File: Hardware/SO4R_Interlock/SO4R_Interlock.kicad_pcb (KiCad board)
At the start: 4 copper layers, 67.4 x 68.6 mm, 120 parts, among them J1 USB-C 2.0 16P, J2 USB-C 2.0 16P, J3 USB-C 2.0 16P, J4 USB-C 2.0 16P, J5 8P8C_LED_Shielded_x4, J7 Header 1x3, U1 FT230XS, U10 TPD4E02B04DQA, U11 TPD4E02B04DQA, U12 TPD4E02B04DQA, U2 FT230XS, U3 74LVC1G07, U4 AVR32DB48x-xPT, U5 FT230XS, U6 FT230XS, U7 74LVC1G07, U8 74LVC1G07, U9 TPD4E02B04DQA

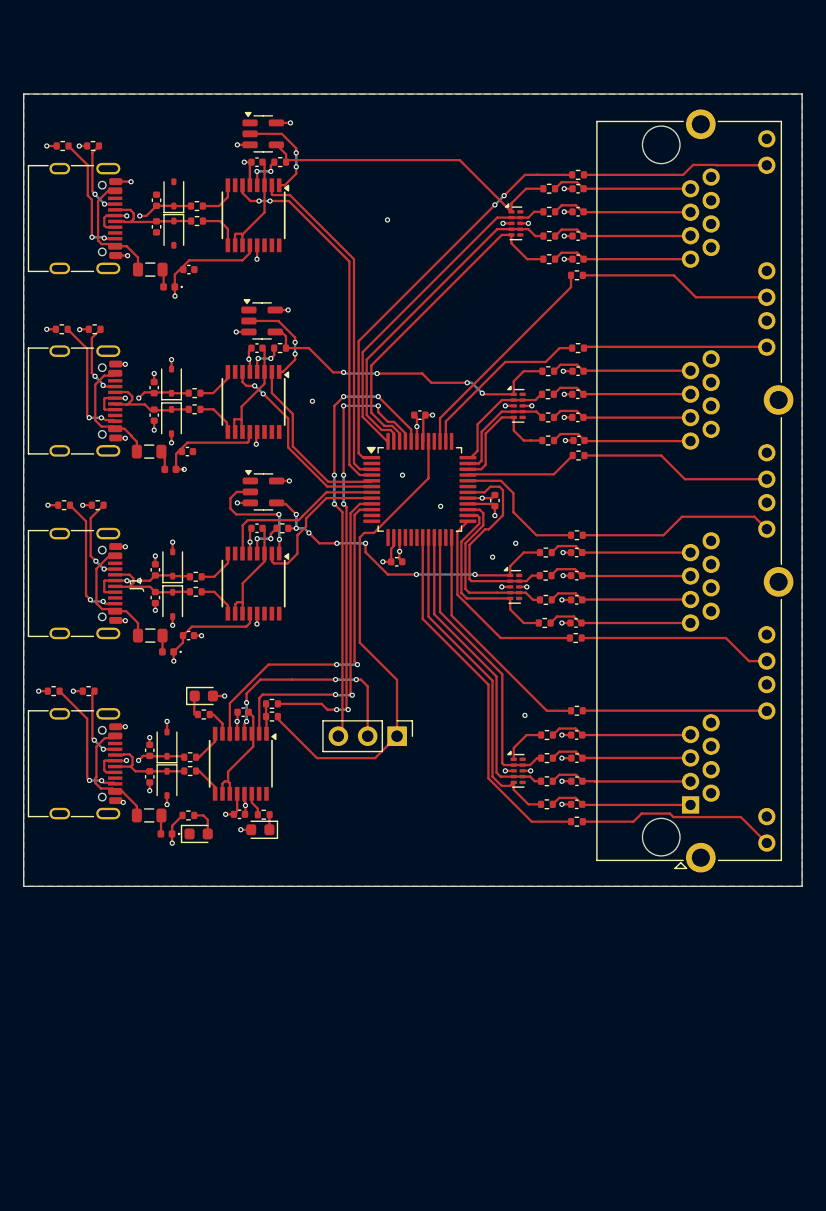
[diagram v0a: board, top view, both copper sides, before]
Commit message: Ordered V1 of Transfer Relay boards and Interlock boards and assembly
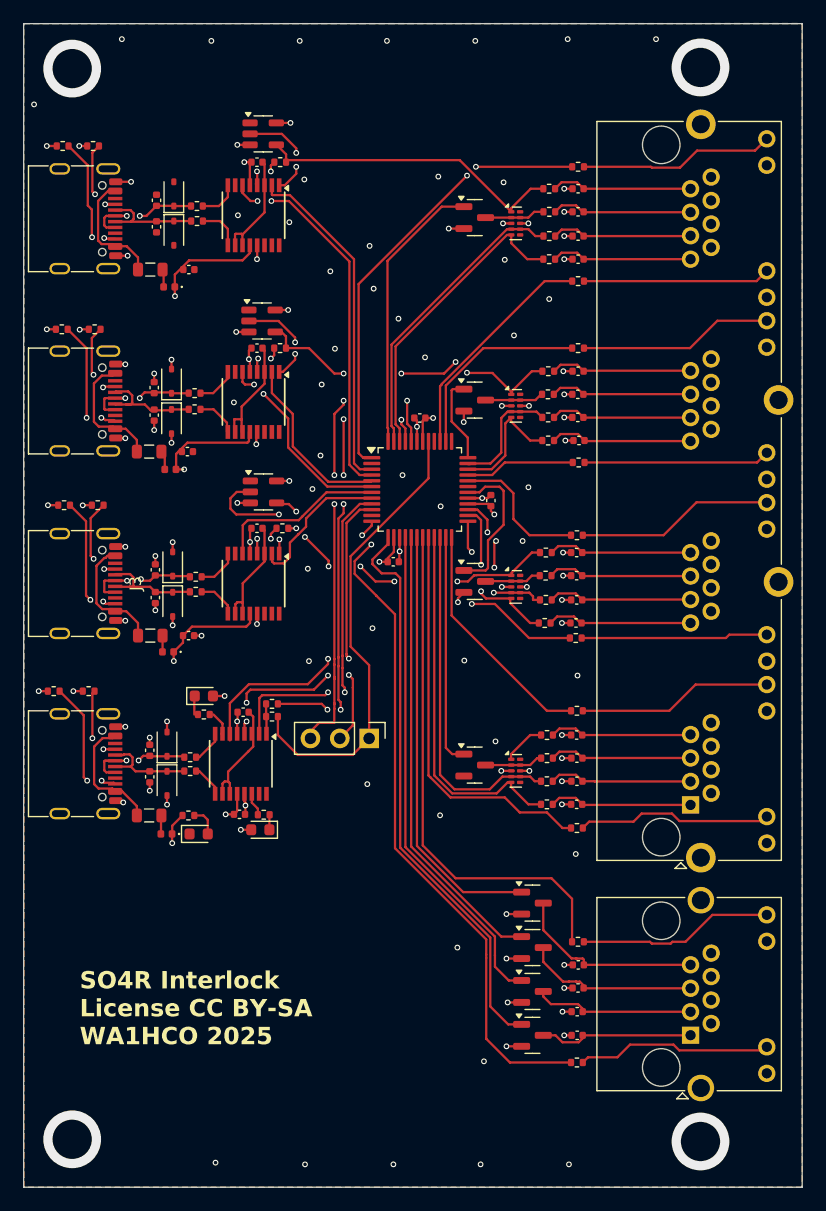
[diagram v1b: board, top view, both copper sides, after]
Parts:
- added C18: .1u, Capacitor_SMD:C_0402_1005Metric, F.Cu at (151.2, 129.5)
- added C19: .1u, Capacitor_SMD:C_0402_1005Metric, F.Cu at (151.2, 131.5)
- added C21: .1u, Capacitor_SMD:C_0402_1005Metric, F.Cu at (151.1, 133.6)
- added C22: .1u, Capacitor_SMD:C_0402_1005Metric, F.Cu at (151.1, 135.6)
- added J6: RJ45_LED_Shielded, Connector_RJ:RJ45_Amphenol_RJHSE538X, F.Cu at (160.9, 135.6)
- added Q1: 2N7002, Package_TO_SOT_SMD:SOT-23, F.Cu at (147.2, 124.2)
- added Q2: 2N7002, Package_TO_SOT_SMD:SOT-23, F.Cu at (147.2, 128.0)
- added Q3: 2N7002, Package_TO_SOT_SMD:SOT-23, F.Cu at (147.2, 131.8)
- added Q4: 2N7002, Package_TO_SOT_SMD:SOT-23, F.Cu at (147.2, 135.6)
- added Q5: 2N7002, Package_TO_SOT_SMD:SOT-23, F.Cu at (142.2, 112.2)
- added Q6: 2N7002, Package_TO_SOT_SMD:SOT-23, F.Cu at (142.2, 64.8)
- added Q7: 2N7002, Package_TO_SOT_SMD:SOT-23, F.Cu at (142.2, 80.6)
- added Q8: 2N7002, Package_TO_SOT_SMD:SOT-23, F.Cu at (142.2, 96.3)
- added R25: 1K, Resistor_SMD:R_0402_1005Metric, F.Cu at (151.1, 137.9)
- added R26: 1K, Resistor_SMD:R_0402_1005Metric, F.Cu at (151.2, 127.5)
- C24: renamed from C35; value .01 -> .1u
- C25: renamed from C28; value .01 -> .1u
- C26: renamed from C20; value .01 -> .1u
- C27: renamed from C25; value .01 -> .1u
- C28: renamed from C29; value .01 -> .1u
- C29: renamed from C30; value .01 -> .1u
- C30: renamed from C22; value .01 -> .1u
- C31: renamed from C24; value .01 -> .1u
- C32, C33: value .01 -> .1u
- C34: renamed from C27; value .01 -> .1u
- C35: renamed from C23; value .01 -> .1u
- C36: renamed from C31; value .01 -> .1u
- C37: renamed from C34; value .01 -> .1u
- C38: renamed from C26; value .01 -> .1u
- C39: renamed from C19; value .01 -> .1u
- D5: renamed from D13; value D_Schottky -> RBQ161QS-40
- R41: renamed from R27; value 33 -> 1K
- moved J5 2.42 mm to (133.1, 109.9)
- moved R44 0.70 mm to (151.2, 60.4)
- moved R45 0.60 mm to (151.2, 86.0)
- moved R49 0.55 mm to (151.1, 117.7)
- moved R43 0.51 mm to (151.2, 70.3)
- moved C17 0.35 mm to (143.7, 89.3)
- moved C20 0.30 mm to (135.2, 94.6)
- moved C23 0.25 mm to (137.5, 82.2)
- moved U10 0.21 mm to (145.8, 81.1)
- moved U12 0.21 mm to (145.8, 112.7)
- moved U11 0.09 mm to (145.8, 96.8)
- turned R47 to 180 degrees
- renumbered C14 to C1, C12 to C10, C16 to C11, C8 to C12, C17 to C13, C15 to C14, C9 to C15, C10 to C16, C21 to C17, C6 to C2, C11 to C20, C13 to C23, C2 to C4, C18 to C5, C5 to C6, C4 to C7, C1 to C8, C7 to C9, D15 to D1, D11 to D10, D6 to D11, D4 to D12, D3 to D13, D2 to D14, D8 to D15, D12 to D2, D5 to D3, D9 to D4, D7 to D6, D1 to D7, D14 to D8, D10 to D9, FB3 to FB1, FB1 to FB3, J4 to J1, J3 to J2, J1 to J3, J2 to J4, J7 to J5, J5 to J7, R8 to R1, R22 to R10, R23 to R11, R20 to R12, R21 to R13, R11 to R14, R18 to R15, R13 to R16, R12 to R17, R14 to R18, R16 to R19, R7 to R2, R10 to R20, R15 to R21, R24 to R22, R19 to R23, R17 to R24, R47 to R27, R43 to R28, R42 to R29, R6 to R3, R41 to R30, R40 to R31, R39 to R32, R38 to R33, R37 to R34, R28 to R35, R29 to R36, R30 to R37, R31 to R38, R32 to R39, R5 to R4, R33 to R40, R25 to R42, R44 to R43, R48 to R44, R46 to R45, R45 to R46, R35 to R47, R34 to R48, R26 to R49, R4 to R5, R36 to R50, R3 to R6, R2 to R7, R1 to R8, U5 to U1, U11 to U10, U10 to U11, U9 to U12, U6 to U2, U1 to U3, U2 to U4, U8 to U5, U7 to U6, U3 to U7, U4 to U8, U12 to U9
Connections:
- net /KEY2 renamed /KEY2\
- net /KEY3 renamed /KEY3\
- net /KEY4 renamed /KEY4\
- J7 pad 10: GND -> Net-(J7-Pad10)
- J7 pad 11: Net-(J5-Pad11) -> GND
- J7 pad 12: GND -> Net-(J7-Pad12)
- J7 pad 21: Net-(J5-Pad21) -> GND
- J7 pad 22: GND -> Net-(J7-Pad22)
- J7 pad 23: Net-(J5-Pad23) -> GND
- J7 pad 24: GND -> Net-(J7-Pad24)
- J7 pad 33: Net-(J5-Pad33) -> GND
- J7 pad 34: GND -> Net-(J7-Pad34)
- J7 pad 35: Net-(J5-Pad35) -> GND
- J7 pad 36: GND -> Net-(J7-Pad36)
- J7 pad 45: Net-(J5-Pad45) -> GND
- J7 pad 46: GND -> Net-(J7-Pad46)
- J7 pad 47: Net-(J5-Pad47) -> GND
- J7 pad 48: GND -> Net-(J7-Pad48)
- J7 pad 9: Net-(J5-Pad9) -> GND
- R28 pad 1: /PTT4 -> /PTT4\
- R32 pad 1: /PTT3 -> /PTT3\
- R36 pad 1: /PTT2 -> /PTT2\
- R40 pad 1: /PTT1 -> /PTT1\
- R41 pad 1: /KEY1 -> /KEY1\
- R43 pad 1: Net-(J5-Pad45) -> Net-(J7-Pad46)
- R44 pad 1: Net-(J5-Pad47) -> Net-(J7-Pad48)
- R45 pad 1: Net-(J5-Pad33) -> Net-(J7-Pad34)
- R46 pad 1: Net-(J5-Pad35) -> Net-(J7-Pad36)
- R47 pad 1: /TX2_LED -> Net-(J7-Pad22)
- R47 pad 2: Net-(J5-Pad21) -> /TX2_LED
- R48 pad 1: Net-(J5-Pad23) -> Net-(J7-Pad24)
- R49 pad 1: Net-(J5-Pad9) -> Net-(J7-Pad10)
- R50 pad 1: Net-(J5-Pad11) -> Net-(J7-Pad12)
- U10 pad 2: /PTT3 -> /PTT3\
- U11 pad 2: /PTT2 -> /PTT2\
- U12 pad 2: /PTT1 -> /PTT1\
- U12 pad 4: /KEY1 -> /KEY1\
- U8 pad 12: unconnected-(U4-PC2-Pad12) -> /TX0
- U8 pad 13: unconnected-(U4-PC3-Pad13) -> /RLY1
- U8 pad 16: unconnected-(U4-PC4-Pad16) -> /RLY2
- U8 pad 17: unconnected-(U4-PC5-Pad17) -> /RLY3
- U8 pad 18: unconnected-(U4-PC6-Pad18) -> /RLY4
- U8 pad 19: /TX1_LED -> /TX1
- U8 pad 20: /SPR1 -> /TX1_LED
- U8 pad 21: /KEY1 -> /SPR1
- U8 pad 22: /PTT1 -> /KEY1\
- U8 pad 23: unconnected-(U4-PD3-Pad23) -> /PTT1
- U9 pad 2: /PTT4 -> /PTT4\
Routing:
- net /TX0: track 0.00 -> 59.0 mm, vias 0 -> 2
- net /RLY1: track 0.00 -> 49.4 mm
- net /TX1: track 0.00 -> 45.2 mm
- net /RLY2: track 0.00 -> 43.2 mm
- net /RLY3: track 0.00 -> 39.5 mm
- net /RLY4: track 0.00 -> 37.4 mm
- net /KEY1\: track 0.00 -> 30.4 mm
- net /KEY1: track 26.7 -> 0.00 mm
- net Net-(J5-Pad9): track 17.3 -> 0.00 mm
- net Net-(J7-Pad24): track 0.00 -> 17.1 mm
- net Net-(J5-Pad23): track 17.0 -> 0.00 mm
- net Net-(J6-Pad12): track 0.00 -> 16.9 mm
- net Net-(J6-Pad10): track 0.00 -> 16.9 mm
- net Net-(J7-Pad48): track 0.00 -> 16.9 mm
- net Net-(J7-Pad10): track 0.00 -> 16.9 mm
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- added copper zone on In1.Cu, net /5V
- added copper zone on In2.Cu, net GND
- removed copper zone on In2.Cu, net /5V
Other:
- board size 67.4 x 68.6 mm -> 67.4 x 100.7 mm
- board text added: "SO4R Interlock License CC BY-SA WA1HCO 2025"

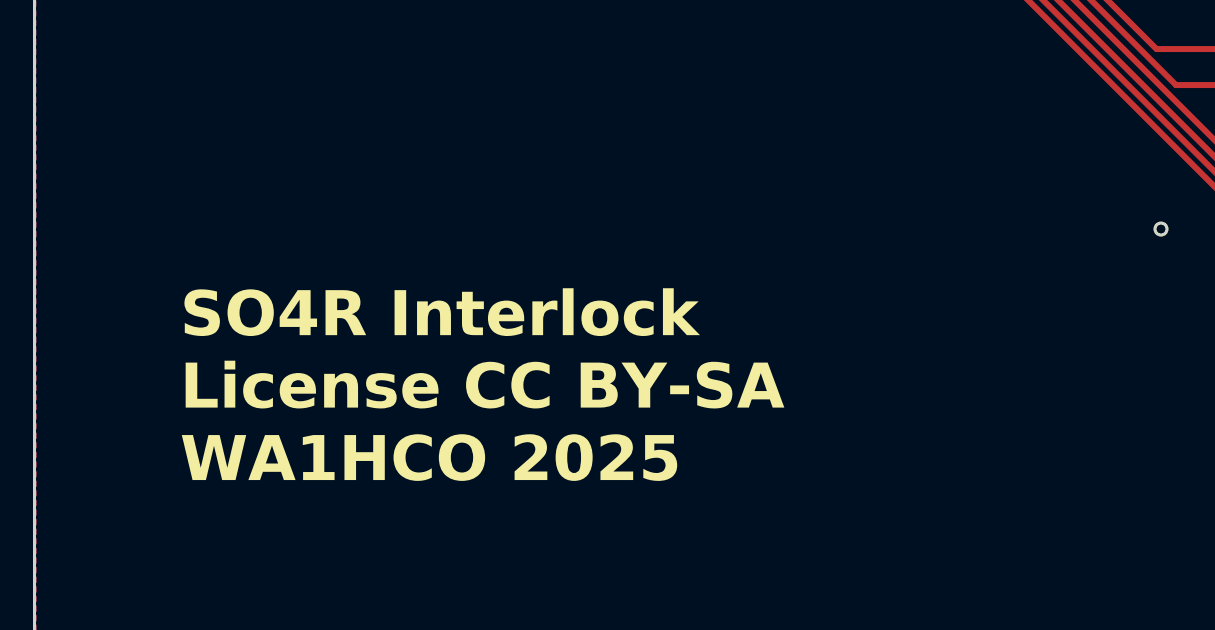
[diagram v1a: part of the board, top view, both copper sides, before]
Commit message: Added drilling dimensions for Transfer Relay enclosure Added ethernet cable color codes to schematic, validated that part Validated KEY/ input to interlock works Validated KEY/ input inhibits lower priority radio and lites Inhibit LED Added rippling LED's to setup() code
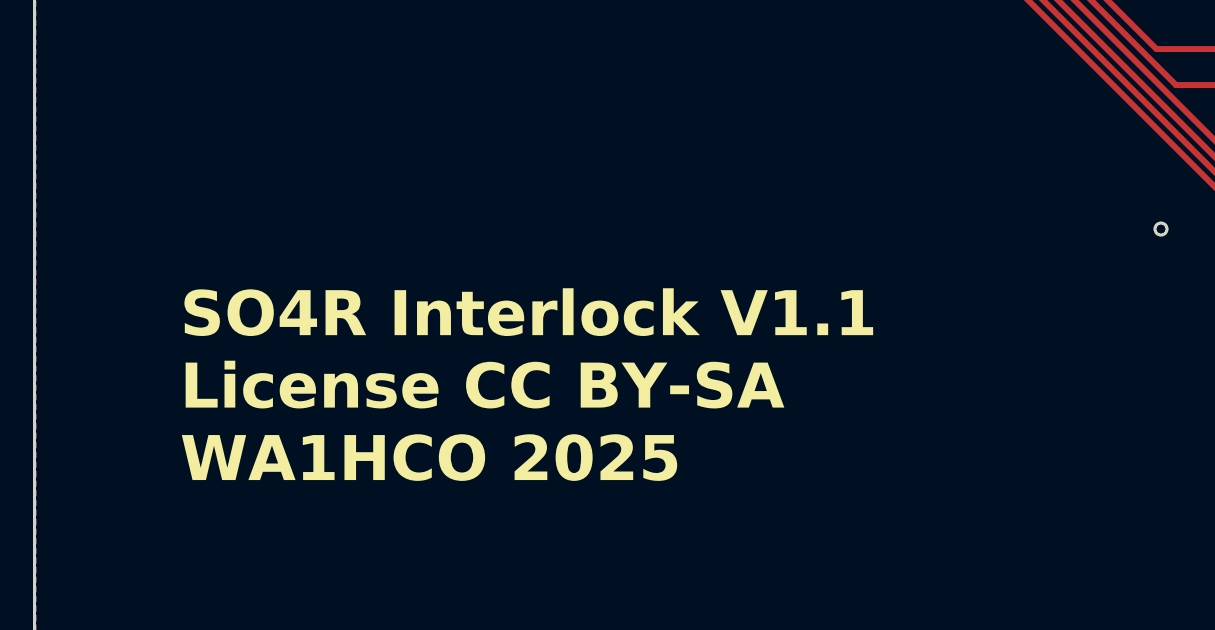
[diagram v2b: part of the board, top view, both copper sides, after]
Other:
- board text added: "SO4R Interlock V1.1 License CC BY-SA WA1HCO 2025"
- board text removed: "SO4R Interlock License CC BY-SA WA1HCO 2025"
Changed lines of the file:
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@@
 		(layer "Edge.Cuts")
 	)
-	(gr_text "SO4R Interlock\nLicense CC BY-SA \nWA1HCO 2025"
+	(gr_text "SO4R Interlock V1.1\nLicense CC BY-SA \nWA1HCO 2025"
 		(at 108.05 136.55 0)
 		(layer "F.SilkS")
